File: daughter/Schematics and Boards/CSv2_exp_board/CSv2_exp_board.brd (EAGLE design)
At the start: 38.1 x 43.8 mm, 144 parts, among them J1 HIROSE-DF40_44-PIN_CONNECTORS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, J2 J-SERIAL-PORT, J3 CORTEX_DEBUG_SMD, J301 HIROSE-DF40_44-PIN_CONNECTORS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, J4 SJ-43514-SMT, J7 J-USB-HIROSE-MICRO-USB, SW1 SPST_TACT-KMR2, SW2 SPST_TACT-KMR2, T1 TPTP10SQ, T10 TPTP10SQ, T11 TPTP10SQ, T2 TPTP10SQ, T3 TPTP10SQ, T4 TPTP10SQ, T5 TPTP10SQ, T6 TPTP10SQ, T7 TPTP10SQ, T8 TPTP10SQ, T9 TPTP10SQ, U1 LOADSWITCH-MIC94164, U10 LOADSWITCH-MIC94164, U11 BMI160, U12 TLV320DAC26IRHB, U13 ADG839YKSZ-500RL7KS_6_ADI-L, U14 LOADSWITCH-MIC94164, U15 LP2980AIM5-2.5/NOPBMF05A_TEX-L, U16 NCP553SQ18T1GSC-82AB_ONS-L, U2 ADA4841-1YRJZ-R7RJ_6-L, U205 MPL3115A2, U3 Value, U4 RFM69HCW, U5 Value, U6 Value, U7 LOADSWITCH-MIC94164, U8 LOADSWITCH-MIC94164, U9 LOADSWITCH-MIC94164, X1 32.768kHz, X2 32.768, X3 uFL, X4 uFL, X5 uFL, X6 uFL

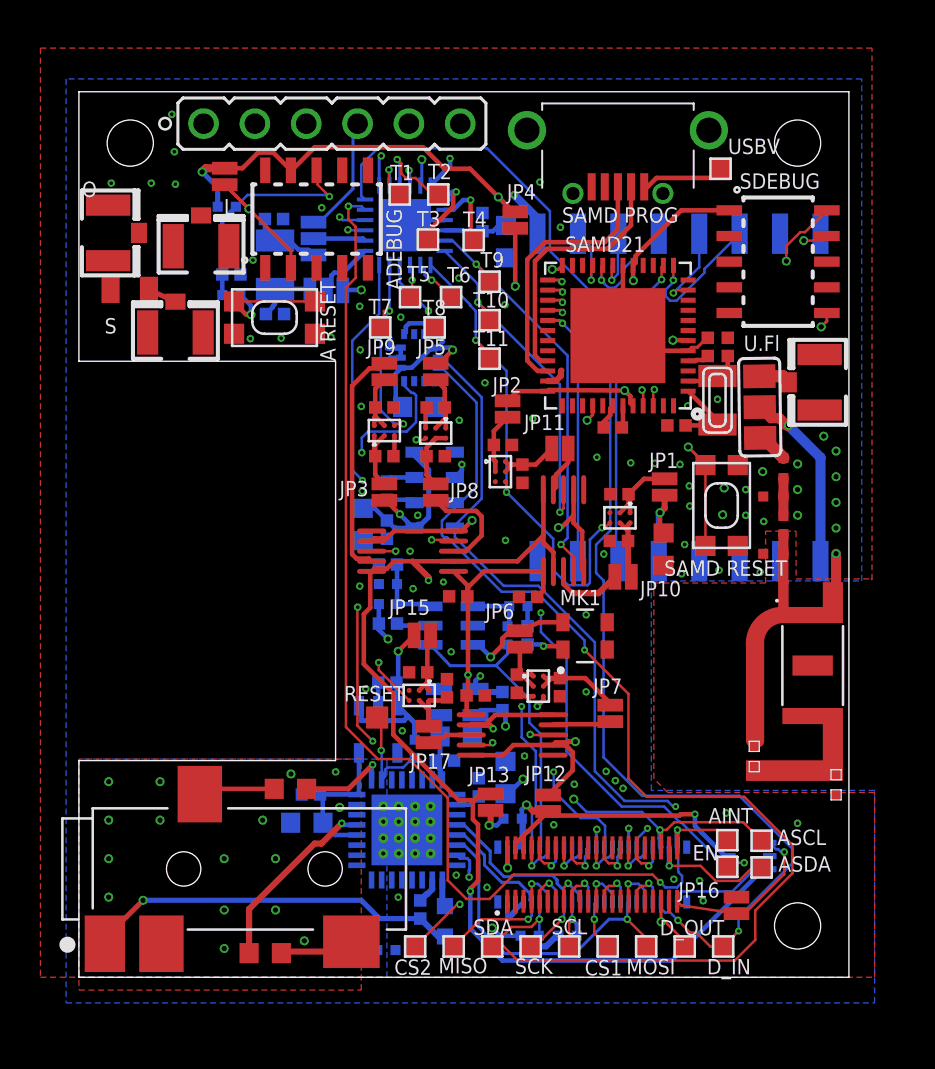
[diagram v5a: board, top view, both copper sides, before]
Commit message: DTR-rounded corners, generated BOM
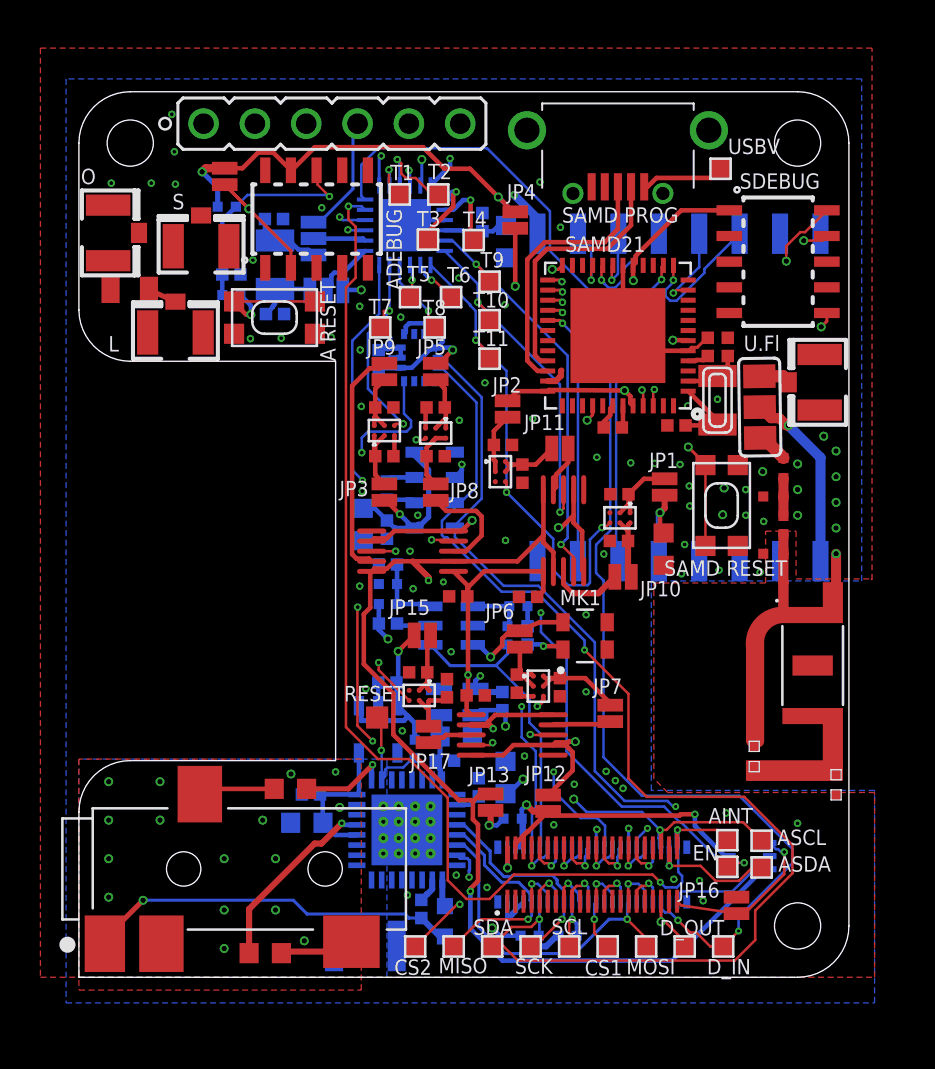
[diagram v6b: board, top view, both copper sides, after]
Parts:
- C25: device Capacitors:C0603 -> Capacitors:C0402
- R12: device Resistors:R0402 -> Resistors:R1210
- moved C25 3.08 mm to (14.8, 30.6), turned to 90 degrees
- moved R12 1.06 mm to (14.2, 1.55)
- moved C33 0.06 mm to (16.9, 3.38)
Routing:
- net +3V3_IMU: track 9.84 -> 8.76 mm
- net GND: track 47.5 -> 48.1 mm
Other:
- outline, holes or cut-outs redrawn

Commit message: DTR-updated BOM
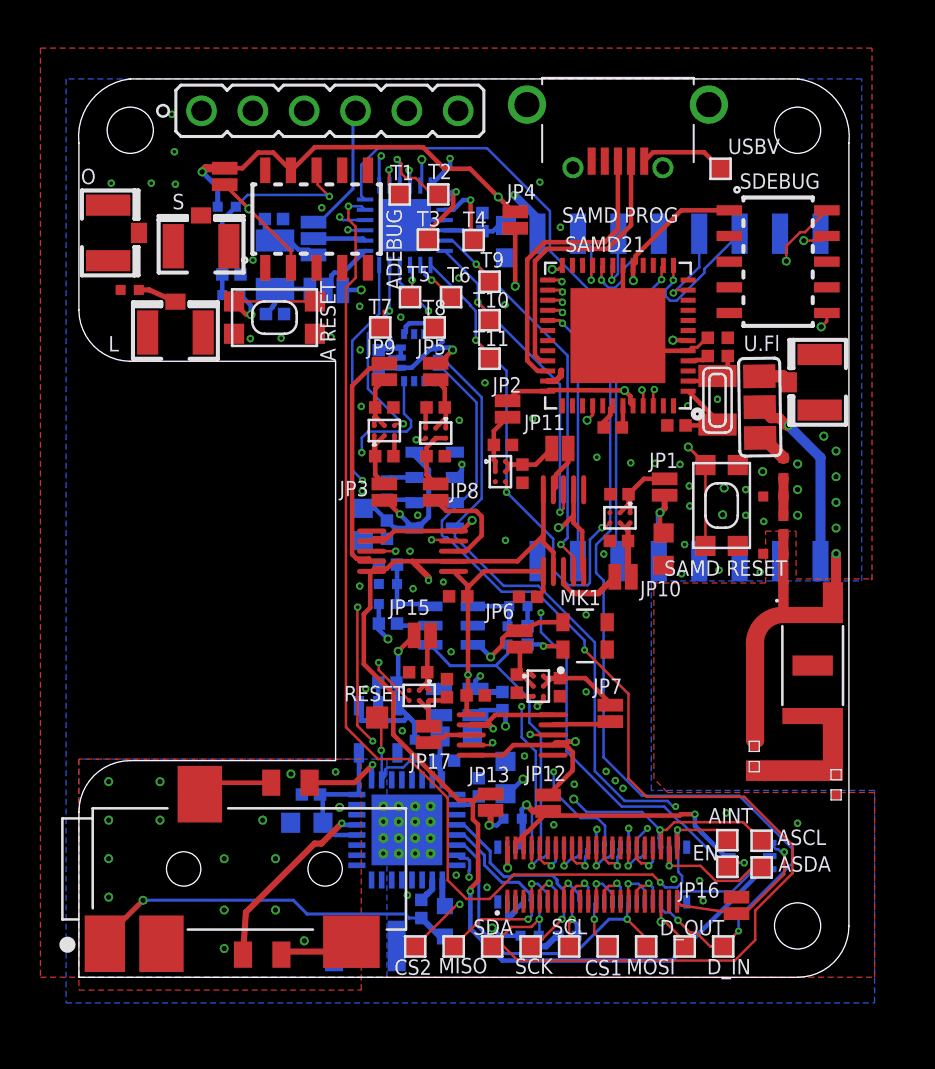
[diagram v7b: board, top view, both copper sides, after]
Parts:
- C31, C32: device Capacitors:C0603 -> Resistors:R0805
- R7: device Resistors:R0805 -> Resistors:R0402
- moved J7 1.27 mm to (26.7, 43.2)
- moved J2 0.64 mm to (12.4, 42.9)
- moved C32 0.30 mm to (10.5, 9.63)
- moved C31 0.17 mm to (9.07, 1.12)
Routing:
- net D_P: track 13.4 -> 14.7 mm
- net D_N: track 12.8 -> 14.1 mm
- net N$3: track 11.0 -> 11.7 mm
- net N$20: track 5.96 -> 6.56 mm
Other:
- board size 38.1 x 43.8 mm -> 38.1 x 44.5 mm

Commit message: DTR-fixed  sch-brd inconsistency problem
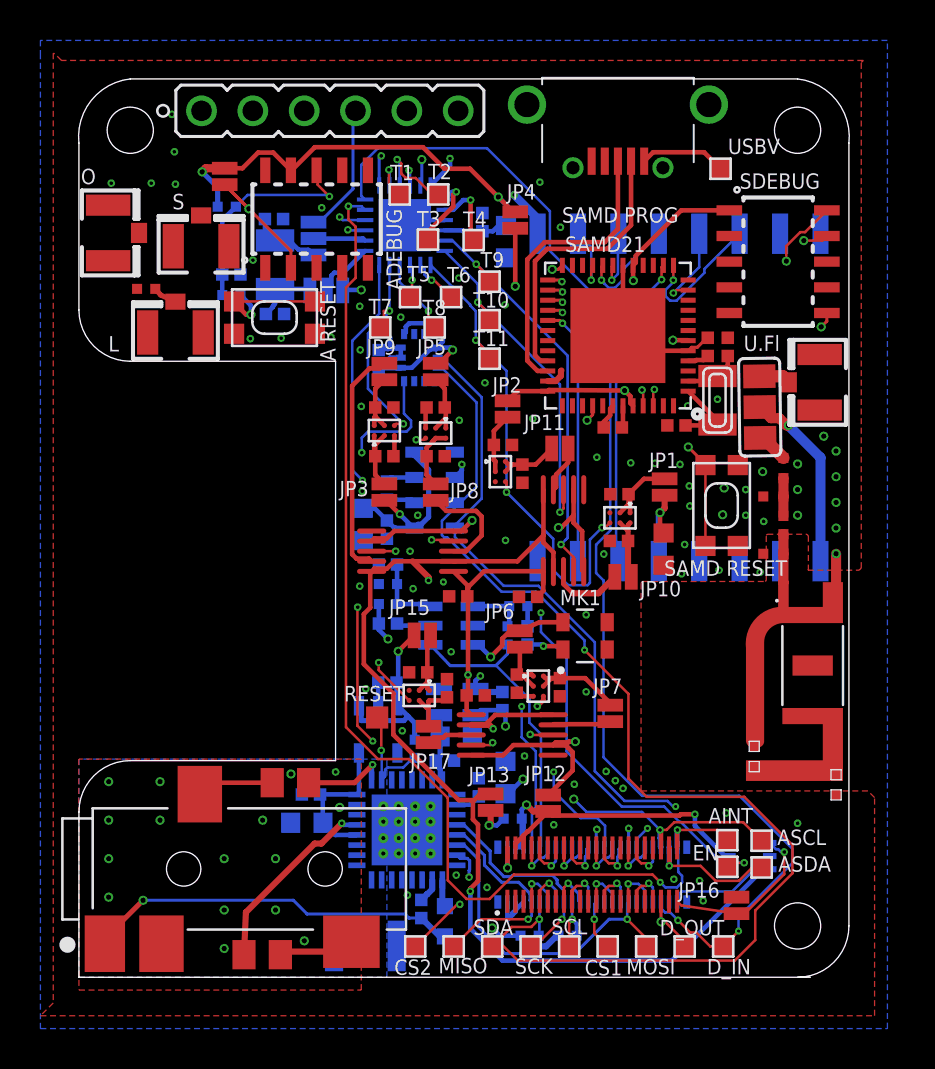
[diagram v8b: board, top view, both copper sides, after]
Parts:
- C31, C32: device Resistors:R0805 -> Capacitors:C0805
- R12: value (none) -> 0R
- R27, R28: value 0 -> 0R
- R7: value 50 -> 50R
- R9: value 39r -> 39R
- R_SENSE: value 1.33 -> 1.33R
- X2: value 32.768 -> 32.768kHz
- moved R7 0.81 mm to (3.33, 34.1)
- renumbered ATTINY-817 to U17, C203 to C47, C204 to C48, J-TAG/UPDI to J6, J301 to J5, U$4 to U19, U205 to U18
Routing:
- net N$11: track 1.94 -> 1.21 mm
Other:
- outline, holes or cut-outs redrawn
